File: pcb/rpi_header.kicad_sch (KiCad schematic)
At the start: 1 part, among them J1 Raspberry_Pi_4

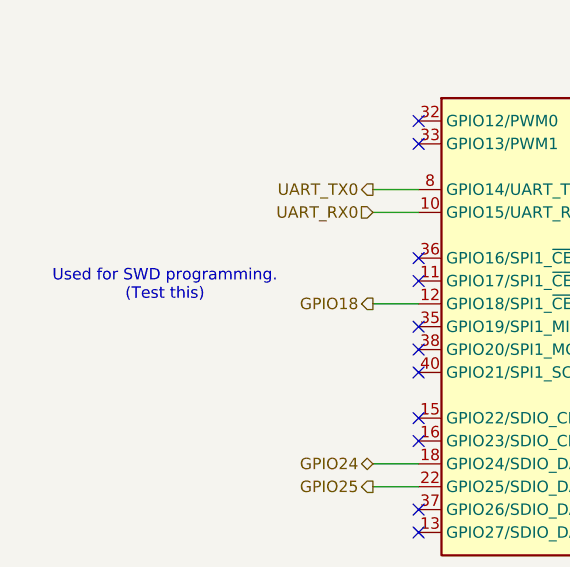
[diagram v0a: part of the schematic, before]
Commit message: Added gerbers, added 2x3 Arduino header.
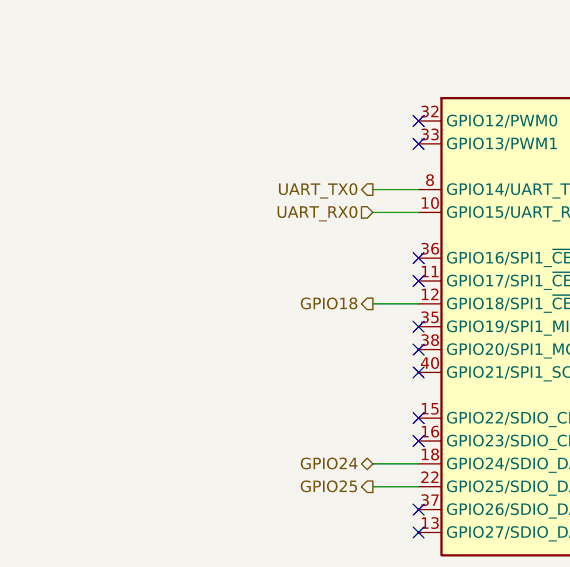
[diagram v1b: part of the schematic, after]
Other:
- note removed: "Used for SWD programming. (Test this)"
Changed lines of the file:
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@@
 	(generator_version "9.0")
 	(paper "A4")
-	(text "Used for SWD programming.\n(Test this)"
-		(exclude_from_sim no)
-		(at 89.916 90.678 0)
-		(effects
-			(font
-				(size 1.27 1.27)
-			)
-		)
-	)
 	(text "Raspberry PI\nPin Header"
 		(exclude_from_sim no)

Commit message: Added remaining part numbers, removed silk for holes, minor touchups
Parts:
- J1: MPN (none) -> NPTC202KFMS-RC
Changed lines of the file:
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@@
+			)
+		)
+		(property "MPN" "NPTC202KFMS-RC"
+			(at 151.13 95.25 0)
+			(effects
+				(font
+					(size 1.27 1.27)
+				)
+				(hide yes)
 			)
 		)

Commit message: R0.1 released
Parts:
- renumbered J1 to J4
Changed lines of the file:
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@@
 		(dnp no)
 		(fields_autoplaced yes)
-		(property "Reference" "#PWR01"
+		(property "Reference" "#PWR035"
 			(at 186.69 71.12 0)
 			(effects
@@
 			(project ""
 				(path "/deaf739e-0e27-4f2f-890a-6dd284a38e9f/b2b53a90-693d-4b74-b6ca-148b5ac29c9a"
-					(reference "#PWR01")
+					(reference "#PWR035")
 					(unit 1)
 				)
@@
 		(dnp no)
 		(fields_autoplaced yes)
-		(property "Reference" "J1"
+		(property "Reference" "J4"
 			(at 151.13 64.77 0)
 			(effects
@@
 			(project "blocky_breakout_pcb"
 				(path "/deaf739e-0e27-4f2f-890a-6dd284a38e9f/b2b53a90-693d-4b74-b6ca-148b5ac29c9a"
-					(reference "J1")
+					(reference "J4")
 					(unit 1)
 				)
@@
 		(dnp no)
 		(fields_autoplaced yes)
-		(property "Reference" "#PWR02"
+		(property "Reference" "#PWR036"
 			(at 151.13 133.35 0)
 			(effects
@@
 			(project ""
 				(path "/deaf739e-0e27-4f2f-890a-6dd284a38e9f/b2b53a90-693d-4b74-b6ca-148b5ac29c9a"
-					(reference "#PWR02")
+					(reference "#PWR036")
 					(unit 1)
 				)
